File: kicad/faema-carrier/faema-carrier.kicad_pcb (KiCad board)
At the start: 2 copper layers, 120 x 95 mm, 41 parts, among them J1 AC_INPUT_220V, J10 NTC_GRUPO, J11 PICO_L, J12 PICO_R, J13 RTD_CALDEIRA, J14 RTD_GRUPO, J2 SSR_CTRL, J3 ENCODER, J4 BUTTONS, J5 LEVEL_PROBE, J6 NEXTION, J7 SPI_DISPLAY, J8 I2C_RTC, J9 NTC_CALDEIRA, Q1 2N7002, U1 HLK-PM05, U2 AMS1117-3.3

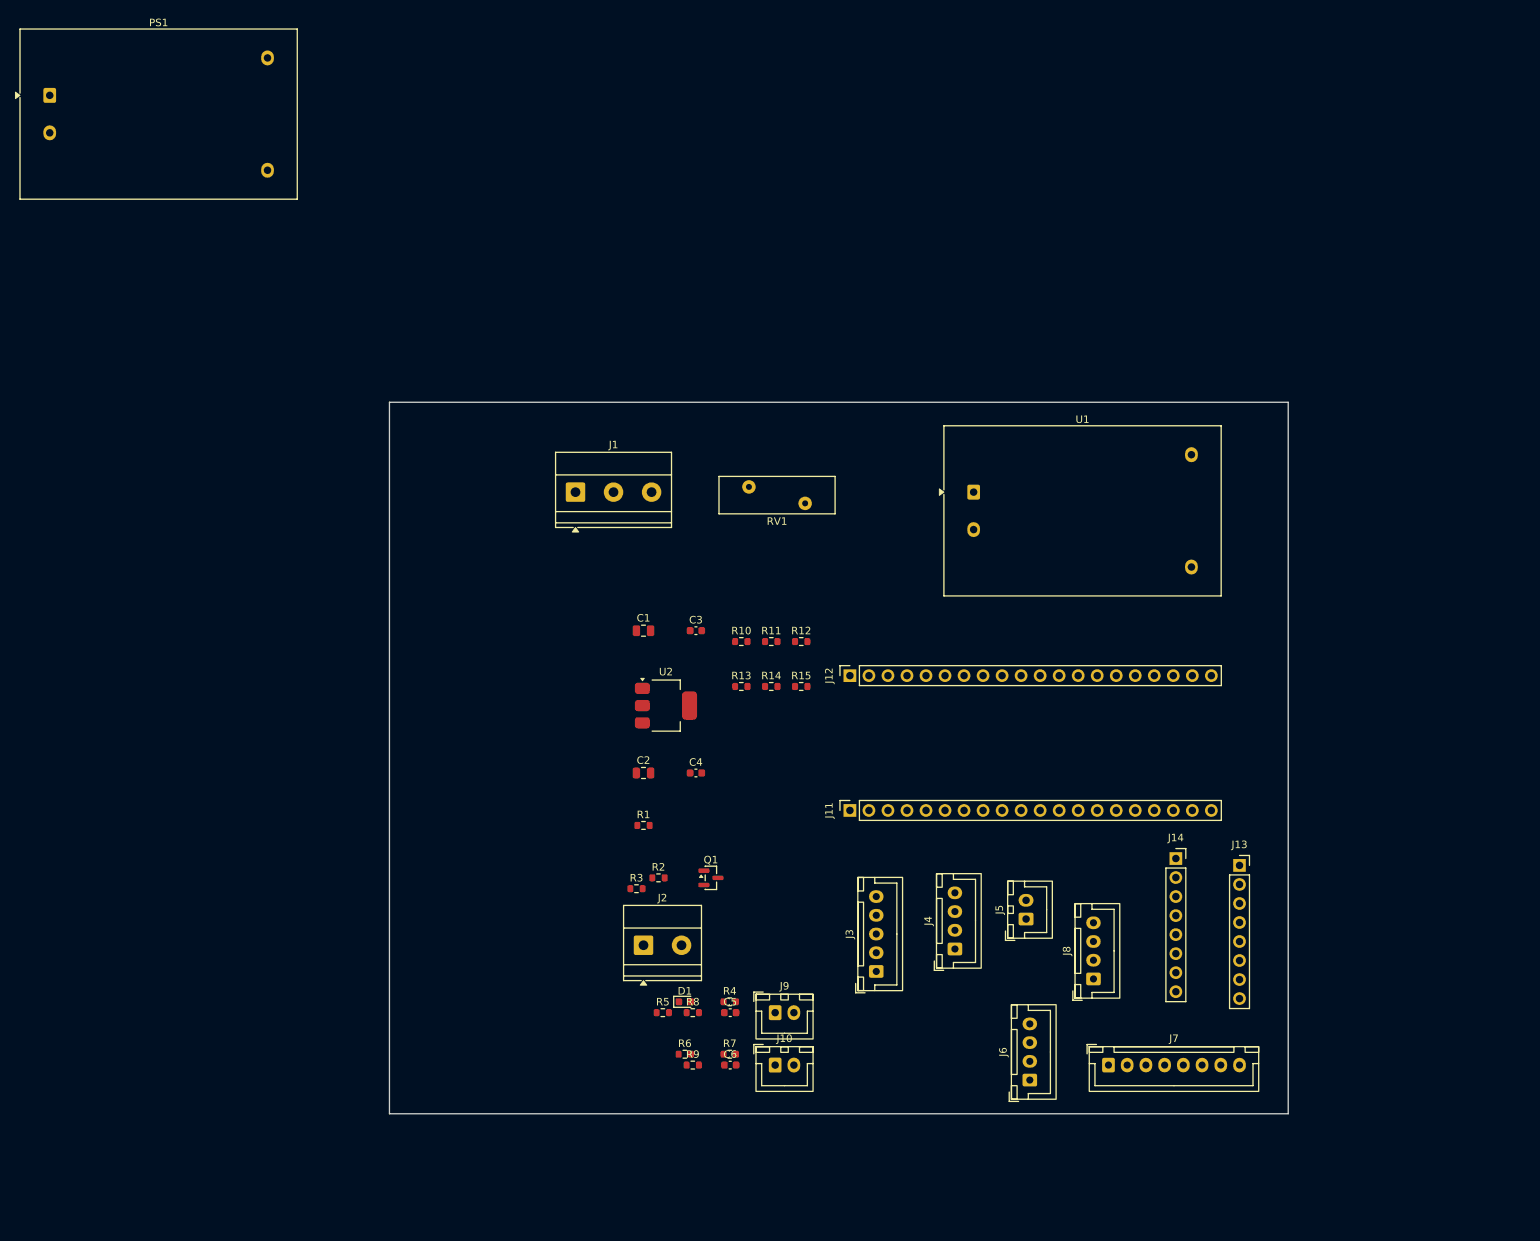
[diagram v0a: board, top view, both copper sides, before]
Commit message: Rev.7: controlador genérico de espresso — MCP23017, SSR dual, bomba MGFR, fluxômetro, pressão
- Arquitetura expandida: 2× SSR, 2× RTD (Adafruit pinout), NTC opcional, sensor pressão
  0-4.5V, fluxômetro (GP21), controle bomba 0-3.3V, 2× sonda nível, 4× saída relé
- MCP23017 (U3 SOIC-28) via I2C: 5 botões, 5 LEDs, 2 níveis, 4 relés, INT→GP22
- Nomes genéricos (RTD1/RTD2, SSR1/SSR2, LEVEL1/2, OUT1-4) — mapeamento da máquina no firmware
- Placa 150×110mm, placement script e BOM/CPL atualizados (0 erros ERC)

Co-Authored-By: Claude Sonnet 4.6 <noreply@anthropic.com>
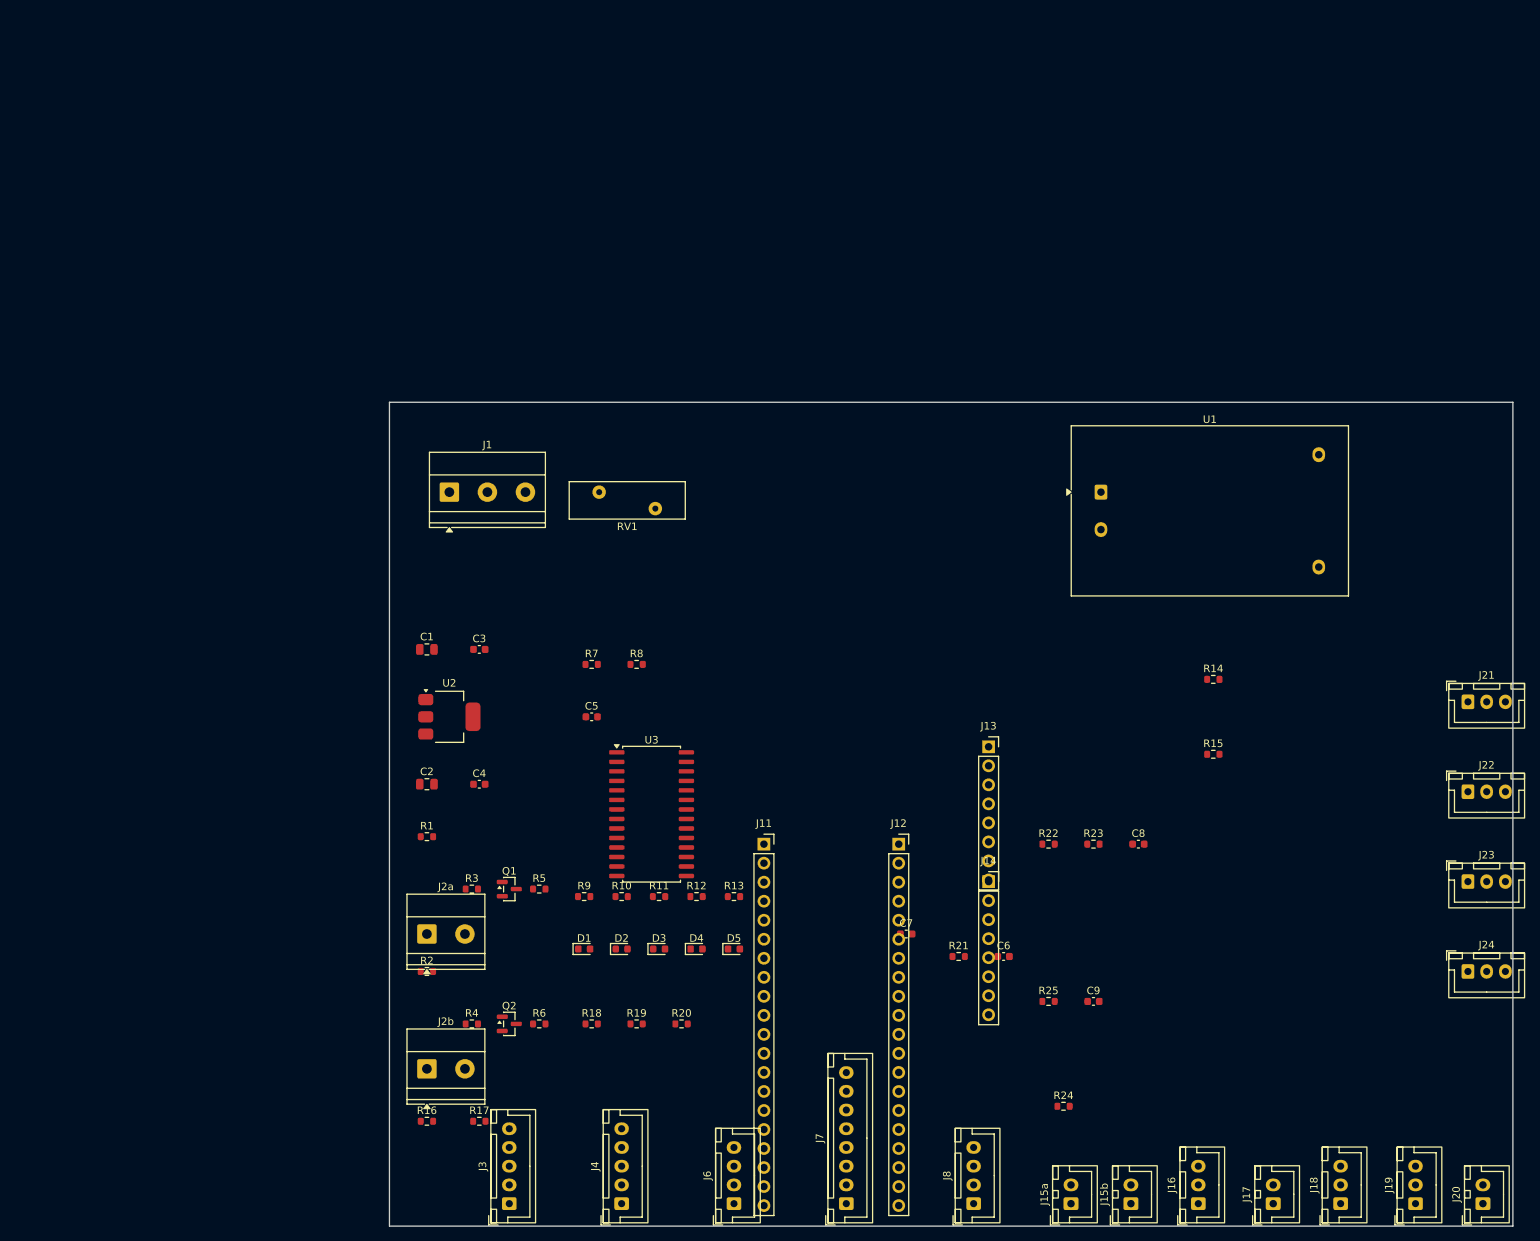
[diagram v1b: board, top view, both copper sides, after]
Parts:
- removed J10: NTC_GRUPO, Connector_JST:JST_XH_B2B-XH-A_1x02_P2.50mm_Vertical
- removed J2: SSR_CTRL, TerminalBlock_Phoenix:TerminalBlock_Phoenix_MKDS-1,5-2-5.08_1x02_P5.08mm_Horizontal
- removed J5: LEVEL_PROBE, Connector_JST:JST_XH_B2B-XH-A_1x02_P2.50mm_Vertical
- removed J9: NTC_CALDEIRA, Connector_JST:JST_XH_B2B-XH-A_1x02_P2.50mm_Vertical
- removed PS1: HLK-PM01, Converter_ACDC:Converter_ACDC_Hi-Link_HLK-PMxx
- added C7: 100nF_50V, Capacitor_SMD:C_0603_1608Metric, F.Cu at (119.0, 121.0)
- added C8: 100nF_50V, Capacitor_SMD:C_0603_1608Metric, F.Cu at (150.0, 109.0)
- added C9: 10nF, Capacitor_SMD:C_0603_1608Metric, F.Cu at (144.0, 130.0)
- added D2: GREEN, LED_SMD:LED_0603_1608Metric, F.Cu at (81.0, 123.0)
- added D3: GREEN, LED_SMD:LED_0603_1608Metric, F.Cu at (86.0, 123.0)
- added D4: GREEN, LED_SMD:LED_0603_1608Metric, F.Cu at (91.0, 123.0)
- added D5: GREEN, LED_SMD:LED_0603_1608Metric, F.Cu at (96.0, 123.0)
- added J15a: LEVEL1, Connector_JST:JST_XH_B2B-XH-A_1x02_P2.50mm_Vertical, F.Cu at (141.0, 157.0)
- added J15b: LEVEL2, Connector_JST:JST_XH_B2B-XH-A_1x02_P2.50mm_Vertical, F.Cu at (149.0, 157.0)
- added J16: FLOW, Connector_JST:JST_XH_B3B-XH-A_1x03_P2.50mm_Vertical, F.Cu at (158.0, 157.0)
- added J17: TEMP_AUX, Connector_JST:JST_XH_B2B-XH-A_1x02_P2.50mm_Vertical, F.Cu at (168.0, 157.0)
- added J18: PRESSURE, Connector_JST:JST_XH_B3B-XH-A_1x03_P2.50mm_Vertical, F.Cu at (177.0, 157.0)
- added J19: ANALOG_IN, Connector_JST:JST_XH_B3B-XH-A_1x03_P2.50mm_Vertical, F.Cu at (187.0, 157.0)
- added J20: PUMP_CTRL, Connector_JST:JST_XH_B2B-XH-A_1x02_P2.50mm_Vertical, F.Cu at (196.0, 157.0)
- added J21: OUT1, Connector_JST:JST_XH_B3B-XH-A_1x03_P2.50mm_Vertical, F.Cu at (194.0, 90.0)
- added J22: OUT2, Connector_JST:JST_XH_B3B-XH-A_1x03_P2.50mm_Vertical, F.Cu at (194.0, 102.0)
- added J23: OUT3, Connector_JST:JST_XH_B3B-XH-A_1x03_P2.50mm_Vertical, F.Cu at (194.0, 114.0)
- added J24: OUT4, Connector_JST:JST_XH_B3B-XH-A_1x03_P2.50mm_Vertical, F.Cu at (194.0, 126.0)
- added J2a: SSR1_OUT, TerminalBlock_Phoenix:TerminalBlock_Phoenix_MKDS-1,5-2-5.08_1x02_P5.08mm_Horizontal, F.Cu at (55.0, 121.0)
- added J2b: SSR2_OUT, TerminalBlock_Phoenix:TerminalBlock_Phoenix_MKDS-1,5-2-5.08_1x02_P5.08mm_Horizontal, F.Cu at (55.0, 139.0)
- added Q2: 2N7002, Package_TO_SOT_SMD:SOT-23, F.Cu at (66.0, 133.0)
- added R16: 10k, Resistor_SMD:R_0603_1608Metric, F.Cu at (55.0, 146.0)
- added R17: 15k, Resistor_SMD:R_0603_1608Metric, F.Cu at (62.0, 146.0)
- added R18: 10k, Resistor_SMD:R_0603_1608Metric, F.Cu at (77.0, 133.0)
- added R19: 10k, Resistor_SMD:R_0603_1608Metric, F.Cu at (83.0, 133.0)
- added R20: 10k, Resistor_SMD:R_0603_1608Metric, F.Cu at (89.0, 133.0)
- added R21: 2k2_0.1%, Resistor_SMD:R_0603_1608Metric, F.Cu at (126.0, 124.0)
- added R22: 33k, Resistor_SMD:R_0603_1608Metric, F.Cu at (138.0, 109.0)
- added R23: 82k, Resistor_SMD:R_0603_1608Metric, F.Cu at (144.0, 109.0)
- added R24: 100R, Resistor_SMD:R_0603_1608Metric, F.Cu at (140.0, 144.0)
- added R25: 10k, Resistor_SMD:R_0603_1608Metric, F.Cu at (138.0, 130.0)
- added U3: MCP23017, Package_SO:SOIC-28W_7.5x17.9mm_P1.27mm, F.Cu at (85.0, 105.0)
- J13: value RTD_CALDEIRA -> RTD1
- J14: value RTD_GRUPO -> RTD2
- J4: footprint Connector_JST:JST_XH_B4B-XH-A_1x04_P2.50mm_Vertical -> Connector_JST:JST_XH_B5B-XH-A_1x05_P2.50mm_Vertical
- R10, R11, R12, R13: value 10k -> 470R
- R14, R15: value 10k -> 100k
- R2: value 100R -> 220R
- R3: value 10k -> 100R
- R4: value 470R -> 100R
- R5: value 100k -> 10k
- R7: value 15k -> 4k7
- R8: value 2k2_0.1% -> 4k7
- R9: value 2k2_0.1% -> 470R
- moved R14 59.0 mm to (160.0, 87.0)
- moved J3 58.0 mm to (66.0, 157.0)
- moved J4 56.0 mm to (81.0, 157.0)
- moved R15 55.8 mm to (160.0, 97.0)
- moved R7 55.2 mm to (77.0, 85.0)
- moved R8 47.1 mm to (83.0, 85.0)
- moved C5 43.6 mm to (77.0, 92.0)
- moved J6 42.8 mm to (96.0, 157.0)
- moved J7 39.6 mm to (111.0, 157.0), turned to 90 degrees
- moved C6 39.3 mm to (132.0, 124.0)
- moved R10 37.6 mm to (81.0, 116.0)
- moved R11 37.2 mm to (86.0, 116.0)
- moved J13 37.1 mm to (130.0, 96.0)
- moved R12 36.8 mm to (91.0, 116.0)
- moved R4 34.6 mm to (61.0, 133.0)
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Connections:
- C5 pad 1: NTC1_ADC -> +3V3
- C6 pad 1: NTC2_ADC -> TEMP_AUX
- D1 pad 1: LED_ANODE -> LED1_A
- J1 pad 3: GND -> PE
- J11 pad 10: (no net) -> SSR1_CTRL
- J11 pad 11: CS_DISP -> SPI_SCK
- J11 pad 12: DC_DISP -> SPI_MOSI
- J11 pad 14: RST_DISP -> CS_DISP
- J11 pad 15: SSR_CTRL -> DC_DISP
- J11 pad 16: LED_STATUS -> RST_DISP
- J12 pad 11: NTC1_ADC -> TEMP_AUX
- J12 pad 12: NTC2_ADC -> PRESSURE
- J12 pad 14: (no net) -> ANALOG_IN
- J12 pad 15: (no net) -> +3V3
- J12 pad 5: BTN1 -> SSR2_CTRL
- J12 pad 6: BTN2 -> PUMP_CTRL
- J12 pad 7: BTN3 -> PULSE_IN
- J12 pad 9: LEVEL_SENSE -> MCP_INT
- J13 pad 1: +5V -> +3V3
- J13 pad 3: SPI_MISO -> (no net)
- J13 pad 4: SPI_MOSI -> SPI_SCK
- J13 pad 5: SPI_SCK -> SPI_MISO
- J13 pad 6: CS_RTD1 -> SPI_MOSI
- J13 pad 7: (no net) -> CS_RTD1
- J14 pad 1: +5V -> +3V3
- J14 pad 3: SPI_MISO -> (no net)
- J14 pad 4: SPI_MOSI -> SPI_SCK
- J14 pad 5: SPI_SCK -> SPI_MISO
- J14 pad 6: CS_RTD2 -> SPI_MOSI
- J14 pad 7: (no net) -> CS_RTD2
- J4 pad 4: GND -> BTN4
- Q1 pad 1: GATE_DRIVE -> GATE1_DRIVE
- Q1 pad 3: SSR_DRIVE -> SSR1_DRIVE
- R1 pad 2: SSR_CTRL_P -> SSR1_CTRL_P
- R10 pad 1: +3V3 -> LED2
- R10 pad 2: BTN1 -> LED2_A
- R11 pad 1: +3V3 -> LED3
- R11 pad 2: BTN2 -> LED3_A
- R12 pad 1: +3V3 -> LED4
- R12 pad 2: BTN3 -> LED4_A
- R13 pad 1: +3V3 -> LED5
- R13 pad 2: ENC_CLK -> LED5_A
- R14 pad 2: ENC_DT -> LEVEL1
- R15 pad 2: ENC_SW -> LEVEL2
- R2 pad 1: SSR_CTRL -> +5V
- R2 pad 2: GATE_DRIVE -> SSR2_CTRL_P
- R3 pad 1: GATE_DRIVE -> SSR1_CTRL
- R3 pad 2: GND -> GATE1_DRIVE
- R4 pad 1: LED_STATUS -> SSR2_CTRL
- R4 pad 2: LED_ANODE -> GATE2_DRIVE
- R5 pad 1: +3V3 -> GATE1_DRIVE
- R5 pad 2: LEVEL_SENSE -> GND
- R6 pad 1: UART_RX_5V -> GATE2_DRIVE
- R6 pad 2: UART_RX -> GND
- R7 pad 1: UART_RX -> +3V3
- R7 pad 2: GND -> I2C_SDA
- R8 pad 2: NTC1_ADC -> I2C_SCL
- R9 pad 1: +3V3 -> LED1
- R9 pad 2: NTC2_ADC -> LED1_A
- U1 pad 1: /AC_L1_FUSED -> AC_L1_FUSED
- U1 pad 2: /AC_L2_FUSED -> AC_L2_FUSED
- U1 pad 3: /+5V -> +5V
- U1 pad 4: (no net) -> GND
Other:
- board size 120 x 95 mm -> 150 x 110 mm
